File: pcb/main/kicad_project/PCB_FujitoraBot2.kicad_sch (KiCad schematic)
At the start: 99 parts, among them IC1 AS5040, IC2 AS5040, J1 MORRO1, SW2 SW_Reset, SW4 SW_Push, U2 LM1117MP-3.3, U3 MPU-6500, Y1 Crystal_GND24

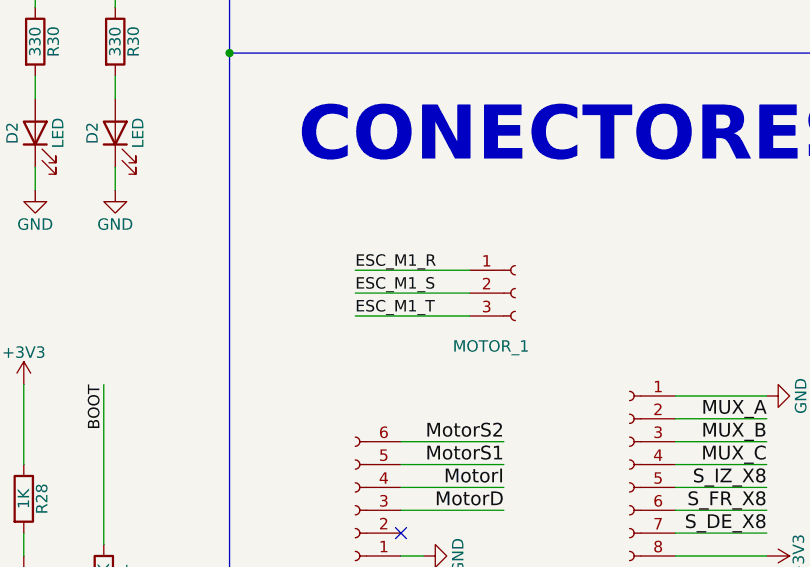
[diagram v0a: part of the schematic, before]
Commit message: Finaliza ruteo y añade etiquetas
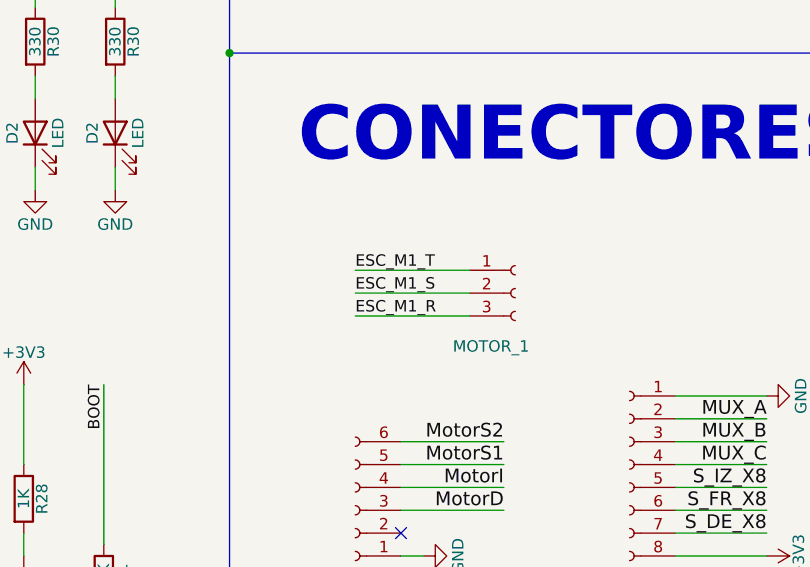
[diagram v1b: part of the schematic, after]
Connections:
- net ESC_M1_R: now also MOTOR_1.3 (Pin_3); no longer MOTOR_1.1 (Pin_1)
- net ESC_M1_T: now also MOTOR_1.1 (Pin_1); no longer MOTOR_1.3 (Pin_3)
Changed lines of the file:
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@@
-		)
-	)
-	(label "ESC_M1_R"
-		(at 349.25 91.44 0)
-		(fields_autoplaced yes)
-		(effects
-			(font
-				(size 1.27 1.27)
-			)
-			(justify left bottom)
 		)
 	)
@@
 		)
 	)
-	(label "ESC_M1_T"
-		(at 349.25 96.52 0)
-		(fields_autoplaced yes)
-		(effects
-			(font
-				(size 1.27 1.27)
-			)
-			(justify left bottom)
-		)
-	)
 	(label "BATT"
 		(at 17.78 259.08 90)
@@
 		)
 	)
+	(label "ESC_M1_T"
+		(at 349.25 91.44 0)
+		(fields_autoplaced yes)
+		(effects
+			(font
+				(size 1.27 1.27)
+			)
+			(justify left bottom)
+		)
+	)
 	(label "SWCLK"
 		(at 53.34 210.82 90)
@@
 		(fields_autoplaced yes)
 		(effects
+			(font
+				(size 1.27 1.27)
+			)
+			(justify left bottom)
+		)
+	)
+	(label "ESC_M1_R"
+		(at 349.25 96.52 0)
+		(fields_autoplaced yes)
+		(effects
